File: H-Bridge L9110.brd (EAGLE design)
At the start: 22.9 x 11.4 mm, 7 parts, among them IC1 L9110S

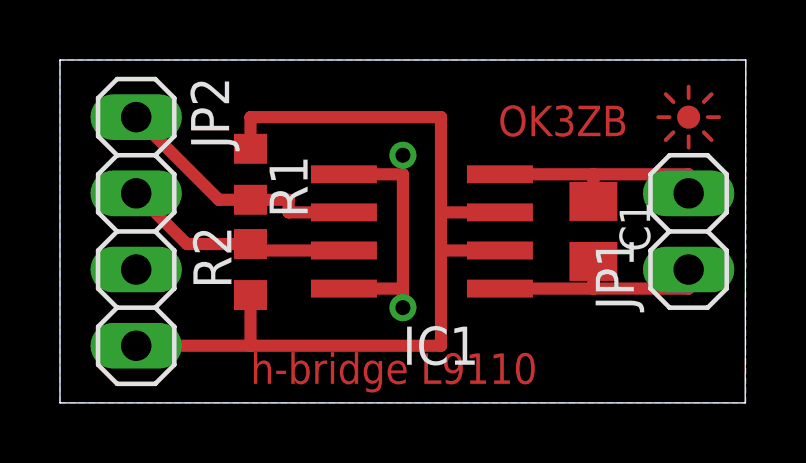
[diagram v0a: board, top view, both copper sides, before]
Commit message: Change visibility of layers
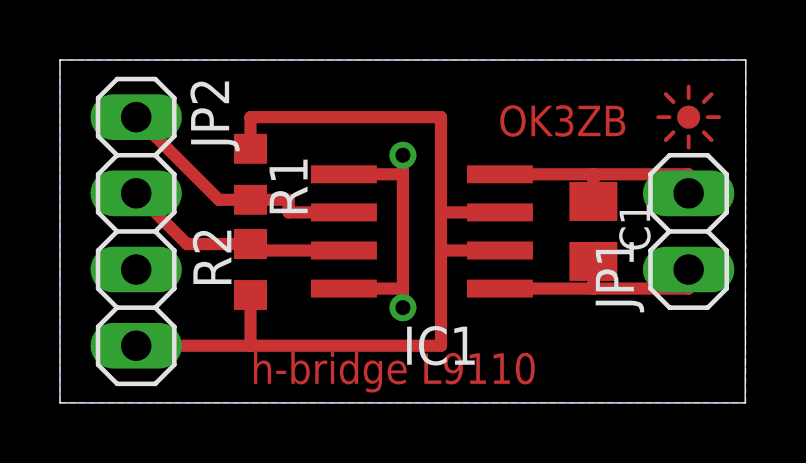
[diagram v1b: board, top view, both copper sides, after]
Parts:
- C1: value 0.1u -> 0.1u (opt)
- R1, R2: value 10k -> 10k (opt)
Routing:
- net GND: track 8.38 -> 9.04 mm, vias 1 -> 2
- net N$1: track 0.03 -> 0.00 mm, vias 1 -> 0
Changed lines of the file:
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@@
 <?xml version="1.0" encoding="utf-8"?>
 <!DOCTYPE eagle SYSTEM "eagle.dtd">
-<eagle version="8.1.1">
+<eagle version="9.0.0">
 <drawing>
 <settings>
 <setting alwaysvectorfont="no"/>
+<setting keepoldvectorfont="yes"/>
 <setting verticaltext="up"/>
 </settings>
@@
 <layer number="23" name="tOrigins" color="15" fill="1" visible="yes" active="yes"/>
 <layer number="24" name="bOrigins" color="15" fill="1" visible="yes" active="yes"/>
-<layer number="25" name="tNames" color="7" fill="1" visible="yes" active="yes"/>
-<layer number="26" name="bNames" color="7" fill="1" visible="yes" active="yes"/>
+<layer number="25" name="tNames" color="7" fill="1" visible="no" active="yes"/>
+<layer number="26" name="bNames" color="7" fill="1" visible="no" active="yes"/>
 <layer number="27" name="tValues" color="7" fill="1" visible="no" active="yes"/>
 <layer number="28" name="bValues" color="7" fill="1" visible="no" active="yes"/>
@@
 <layer number="37" name="tTest" color="7" fill="1" visible="no" active="yes"/>
 <layer number="38" name="bTest" color="7" fill="1" visible="no" active="yes"/>
-<layer number="39" name="tKeepout" color="4" fill="11" visible="yes" active="yes"/>
-<layer number="40" name="bKeepout" color="1" fill="11" visible="yes" active="yes"/>
-<layer number="41" name="tRestrict" color="4" fill="10" visible="yes" active="yes"/>
-<layer number="42" name="bRestrict" color="1" fill="10" visible="yes" active="yes"/>
-<layer number="43" name="vRestrict" color="2" fill="10" visible="yes" active="yes"/>
+<layer number="39" name="tKeepout" color="4" fill="11" visible="no" active="yes"/>
+<layer number="40" name="bKeepout" color="1" fill="11" visible="no" active="yes"/>
+<layer number="41" name="tRestrict" color="4" fill="10" visible="no" active="yes"/>
+<layer number="42" name="bRestrict" color="1" fill="10" visible="no" active="yes"/>
+<layer number="43" name="vRestrict" color="2" fill="10" visible="no" active="yes"/>
 <layer number="44" name="Drills" color="7" fill="1" visible="no" active="yes"/>
 <layer number="45" name="Holes" color="7" fill="1" visible="yes" active="yes"/>
@@
 <text x="20.955" y="2.54" size="1.016" layer="125" font="fixed">Oa</text>
 <text x="20.955" y="8.255" size="1.016" layer="125" font="fixed">Ob</text>
-<text x="14.605" y="8.89" size="1.016" layer="1" font="fixed">OK3ZB</text>
-<text x="6.35" y="0.635" size="1.016" layer="1" font="fixed">h-bridge L9110</text>
+<text x="14.605" y="8.89" size="1.016" layer="1" font="vector">OK3ZB</text>
+<text x="6.35" y="0.635" size="1.016" layer="1" font="vector">h-bridge L9110</text>
 <text x="18.655003125" y="6.714996875" size="1.016" layer="125" font="fixed" rot="R270">C1</text>
 <text x="15.24" y="3.175" size="1.27" layer="125" font="fixed" rot="R180">IC1</text>
@@
 <param name="mdSmdStop" value="0mil"/>
 <param name="msWidth" value="10mil"/>
-<param name="msDrill" value="24mil"/>
+<param name="msDrill" value="0.5mm"/>
 <param name="msMicroVia" value="9.99mm"/>
 <param name="msBlindViaRatio" value="0.5"/>
@@
 <param name="dpMaxLengthDifference" value="10mm"/>
 <param name="dpGapFactor" value="2.5"/>
-<param name="checkGrid" value="0"/>
 <param name="checkAngle" value="0"/>
 <param name="checkFont" value="1"/>
 <param name="checkRestrict" value="1"/>
+<param name="checkStop" value="0"/>
+<param name="checkValues" value="0"/>
 <param name="useDiameter" value="13"/>
 <param name="maxErrors" value="50"/>
@@
 </autorouter>
 <elements>
-<element name="C1" library="rcl" package="C0805K" value="0.1u" x="17.78" y="5.715" rot="R270"/>
+<element name="C1" library="rcl" package="C0805K" value="0.1u (opt)" x="17.78" y="5.715" rot="R270"/>
 <element name="IC1" library="h-bridge" package="SO8" value="L9110S" x="12.065" y="5.715" rot="R90"/>
 <element name="JP1" library="pinhead" package="1X02" value="OUT" x="20.955" y="5.715" rot="R90"/>
 <element name="JP2" library="pinhead" package="1X04" value="IN" x="2.54" y="5.715" rot="R270"/>
-<element name="R1" library="rcl" package="R0603" value="10k" x="6.35" y="7.62" rot="R270"/>
-<element name="R2" library="rcl" package="R0603" value="10k" x="6.35" y="4.445" rot="R90"/>
+<element name="R1" library="rcl" package="R0603" value="10k (opt)" x="6.35" y="7.62" rot="R270"/>
+<element name="R2" library="rcl" package="R0603" value="10k (opt)" x="6.35" y="4.445" rot="R90"/>
 <element name="PICTO1" library="My_Picto" package="PICTO_1" value="PICTO_1" x="20.955" y="9.525"/>
 </elements>
@@
 <wire x1="11.43" y1="3.81" x2="11.43" y2="3.175" width="0.4064" layer="1"/>
 <via x="11.43" y="3.175" extent="1-16" drill="0.5"/>
+<wire x1="11.43" y1="7.62" x2="11.43" y2="8.255" width="0.4064" layer="1"/>
+<via x="11.43" y="8.255" extent="1-16" drill="0.5"/>
+<wire x1="11.43" y1="8.255" x2="11.43" y2="8.2296" width="0.4064" layer="1"/>
 </signal>
 <signal name="VCC">
@@
 <wire x1="4.23" y1="5.295" x2="6.35" y2="5.295" width="0.4064" layer="1"/>
 </signal>
-<signal name="N$1">
-<via x="11.43" y="8.255" extent="1-16" drill="0.5"/>
-<wire x1="11.43" y1="8.255" x2="11.43" y2="8.2296" width="0.4064" layer="1"/>
-</signal>
 </signals>
